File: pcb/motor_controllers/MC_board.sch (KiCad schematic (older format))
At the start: 22 parts, among them J1 Screw_Terminal_01x08, U1 Teensy3.2

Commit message: Added analog output RJ45 and audio amplifier symbol.
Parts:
- removed 5VGNDTEST1, 5VTEST1, 9VGNDTEST1, 9VTEST1: TestPoint, TestPoint:TestPoint_Plated_Hole_D5.0mm, symbol Connector:TestPoint
- removed C2, C3, C4: 100 uF, Capacitor_THT:C_Rect_L7.2mm_W7.2mm_P5.00mm_FKS2_FKP2_MKS2_MKP2, symbol Device:CP1
- added 12V1: 12V, Connector_BarrelJack:BarrelJack_Horizontal, symbol Connector:Barrel_Jack
- added J2: RJ45, symbol Connector:RJ45
- added U2: MAX98306, spatialsparrow:MAX98306, symbol spatialsparrow:MAX98306
- 5V1: value Barrel_Jack -> 5V
- 9V1: value Barrel_Jack -> 9V
- U1: footprint Teensey:Teensy30_31_32_LC -> lib:Teensy30_31_32_LC; symbol teensey:Teensy3.2 -> teensy:Teensy3.2
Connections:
- net labels added: +5V, +9V, GND
- wire segments 213 -> 146
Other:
- note added: "Power connectors\n"
- note added: "Stimuli - analog output connection"
- note added: "Teensy controller and stepper motor drivers"
- moved on the sheet: 5V1, 9V1, C1, FromTouch1, FromZeros1, J1, LeverL-ToMotor1, LeverR-ToMotor1, MC-LeverL1, MC-LeverR1, MC-SpoutL1, MC-SpoutR1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

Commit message: Added pinout text to kicad
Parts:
- renumbered LeverL-ToMotor1 to HandleL-ToMotor1, LeverR-ToMotor1 to HandleR-ToMotor1
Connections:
- net at MC-SpoutR1.3 (A2): now also MC-SpoutR1.4 (A1), SpoutR-ToMotor1.1 (Pin_1); no longer SpoutR-ToMotor1.2 (Pin_2)
- net at HandleR-ToMotor1.2 (Pin_2), MC-LeverR1.3 (A2): now also HandleR-ToMotor1.4 (Pin_4), MC-LeverR1.4 (A1), MC-LeverR1.6 (B2)
- net at HandleR-ToMotor1.1 (Pin_1): now also HandleR-ToMotor1.3 (Pin_3), MC-LeverR1.5 (B1); no longer MC-LeverR1.4 (A1)
- net at J1.7 (Pin_7), U1.27 (20_A6_CS_PWM): now also FromTouch1.1 (Pin_1), U1.30 (23_A9_Touch_PWM)
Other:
- note added: "INPUT PINS\n// Inputs for lick sensors\nLEVERSENSOR_L 15 // touch line for lever touch\nLEVERSENSOR_R 16 // touch line for lever touch\nSPOUTSENSOR_L 22 // touch line for left spout\nSPOUTSENSOR_R 23 // touch line for right spout\n// Pins for stepper - spouts\nPIN_SPOUTOUT_L 5\nPIN_SPOUTOUT_R 6\nPIN_SPOUTSTEP_L 13\nPIN_SPOUTDIR_L 14\nPIN_SPOUTSTEP_R 17\nPIN_SPOUTDIR_R 18\n// Pins for stepper - ha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"
- note added: "Stepper motor drivers\nHandles and Spout motors\n"
- note removed: "Teensy controller and stepper motor drivers"
- moved on the sheet: HandleL-ToMotor1, HandleR-ToMotor1, MC-LeverL1, MC-LeverR1, MC-SpoutL1, MC-SpoutR1, SpoutL-ToMotor1, SpoutR-ToMotor1, U1

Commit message: Pinout added and rj45
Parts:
- added J?: Screw_Terminal_01x02, symbol Connector:Screw_Terminal_01x02
- added SoundVision: Screw_Terminal_01x06, TerminalBlock_TE-Connectivity:TerminalBlock_TE_282825-4_1x06_P5.08mm_Horizontal, symbol Connector:Screw_Terminal_01x05
- FromTouch1, FromZeros1: symbol Connector:Screw_Terminal_01x04 -> Connector:Screw_Terminal_01x05
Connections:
- net at MC-SpoutL1.15 (STEP): no longer U1.20 (13_LED_SCK)
- net at MC-SpoutL1.16 (DIR): no longer U1.21 (14_A0_SCK)
- net at MC-SpoutL1.3 (A2): no longer SpoutL-ToMotor1.2 (Pin_2)
- net at MC-SpoutL1.4 (A1): no longer SpoutL-ToMotor1.1 (Pin_1)
- net at MC-SpoutL1.5 (B1): no longer SpoutL-ToMotor1.3 (Pin_3)
- net at MC-SpoutL1.6 (B2): no longer SpoutL-ToMotor1.4 (Pin_4)
- net at MC-SpoutR1.15 (STEP): no longer U1.24 (17_A3_SDA0_Touch)
- net at MC-SpoutR1.16 (DIR): no longer U1.25 (18_A4_SDA0_Touch)
- net at MC-SpoutR1.5 (B1): no longer SpoutR-ToMotor1.3 (Pin_3)
- net at MC-SpoutR1.6 (B2): no longer SpoutR-ToMotor1.4 (Pin_4)
- net at MC-LeverL1.15 (STEP): no longer U1.12 (10_TX2_CS_PWM)
- net at MC-LeverL1.3 (A2): no longer HandleL-ToMotor1.2 (Pin_2)
- net at MC-LeverL1.4 (A1): no longer HandleL-ToMotor1.1 (Pin_1)
- net at MC-LeverL1.5 (B1): no longer HandleL-ToMotor1.3 (Pin_3)
- net at MC-LeverL1.6 (B2): no longer HandleL-ToMotor1.4 (Pin_4)
- net at MC-LeverL1.9 (~EN): no longer U1.11 (9_RX2_CS_PWM)
- net at MC-LeverR1.15 (STEP): no longer U1.13 (11_DOUT)
- net at MC-LeverR1.16 (DIR): no longer U1.14 (12_DIN)
- net at U1.10 (8_TX3_DIN): no longer FromZeros1.1 (Pin_1)
- net at U1.2 (0_RX1_Touch): no longer J1.1 (Pin_1)
- net at U1.22 (15_A1_CS_Touch): no longer FromTouch1.4 (Pin_4)
- net at U1.23 (16_A2_SCL0_Touch): no longer FromTouch1.3 (Pin_3)
- net at U1.26 (19_A5_SCL0_Touch): no longer J1.6 (Pin_6)
- net at U1.28 (21_A7_RX1_CS_PWM): no longer J1.8 (Pin_8)
- net at U1.29 (22_A8_Touch_PWM): no longer FromTouch1.2 (Pin_2)
- net at U1.3 (1_TX1_Touch): no longer J1.2 (Pin_2)
- net at U1.4 (2): no longer J1.3 (Pin_3)
- net at U1.5 (3_TX_PWM): no longer J1.4 (Pin_4)
- net at U1.6 (4_RX_PWM): no longer J1.5 (Pin_5)
- net at U1.7 (5_TX1_PWM): no longer FromZeros1.4 (Pin_4)
- net at U1.8 (6_PWM): no longer FromZeros1.3 (Pin_3)
- net at U1.9 (7_RX3_DOUT): no longer FromZeros1.2 (Pin_2)
- now unconnected: FromTouch1.1 (Pin_1), HandleR-ToMotor1.1 (Pin_1), HandleR-ToMotor1.2 (Pin_2), HandleR-ToMotor1.3 (Pin_3), HandleR-ToMotor1.4 (Pin_4), J1.7 (Pin_7), MC-LeverR1.3 (A2), MC-LeverR1.4 (A1), MC-LeverR1.5 (B1), MC-LeverR1.6 (B2), MC-SpoutR1.3 (A2), MC-SpoutR1.4 (A1), SpoutR-ToMotor1.1 (Pin_1), U1.27 (20_A6_CS_PWM), U1.30 (23_A9_Touch_PWM)
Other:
- moved on the sheet: C1, HandleL-ToMotor1, HandleR-ToMotor1, MC-LeverL1, MC-LeverR1, MC-SpoutL1, MC-SpoutR1, SpoutL-ToMotor1, SpoutR-ToMotor1

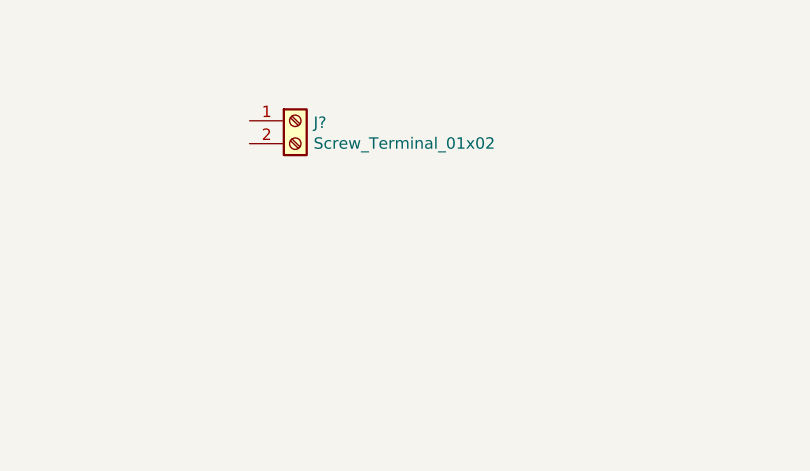
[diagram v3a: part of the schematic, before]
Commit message: text on screw terminal
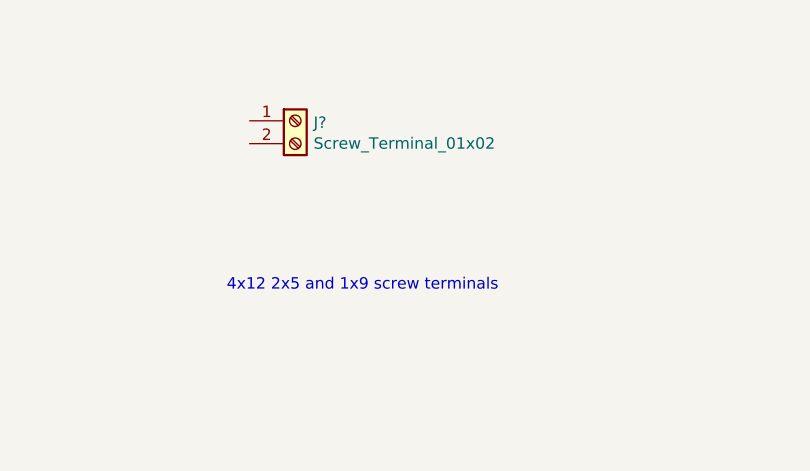
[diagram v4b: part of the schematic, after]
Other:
- note added: "4x12 2x5 and 1x9 screw terminals"
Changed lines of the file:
@@
 	1    0    0    -1
 $EndComp
+Text Notes 5000 13350 0    50   ~ 0
+4x12 2x5 and 1x9 screw terminals
 $EndSCHEMATC

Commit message: ran connections and did board layout
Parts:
- removed J1: Screw_Terminal_01x08, symbol Connector:Screw_Terminal_01x08
- added J12V1, J12V3, J12V4, J5V1, J5V2, J9V1: Screw_Terminal_01x02, teensey:TerminalBlock_TE_282825-2_1x02_P5.08mm_Horizontal, symbol Connector:Screw_Terminal_01x02
- added SoundVisionL1: Screw_Terminal_01x06, teensey:TerminalBlock_TE_282825-6_1x06_P5.08mm_Horizontal, symbol Connector:Screw_Terminal_01x06
- added sync_trigger_out1: Screw_Terminal_01x05, teensey:TerminalBlock_TE_282825-5_1x05_P5.08mm_Horizontal, symbol Connector:Screw_Terminal_01x05
- HandleL-ToMotor1, HandleR-ToMotor1, SpoutL-ToMotor1, SpoutR-ToMotor1: footprint TerminalBlock_TE-Connectivity:TerminalBlock_TE_282825-4_1x04_P5.08mm_Horizontal -> teensey:TerminalBlock_TE_282825-4_1x04_P5.08mm_Horizontal
- J12V2: renamed from J?; footprint (none) -> teensey:TerminalBlock_TE_282825-2_1x02_P5.08mm_Horizontal
- J2: footprint (none) -> teensey:RJ45_sparkfun
- SoundVisionR1: renamed from SoundVision; footprint TerminalBlock_TE-Connectivity:TerminalBlock_TE_282825-4_1x06_P5.08mm_Horizontal -> teensey:TerminalBlock_TE_282825-6_1x06_P5.08mm_Horizontal; symbol Connector:Screw_Terminal_01x05 -> Connector:Screw_Terminal_01x06
- ToHandleL1: renamed from FromZeros1; value Screw_Terminal_01x04 -> Screw_Terminal_01x05; footprint TerminalBlock_TE-Connectivity:TerminalBlock_TE_282825-4_1x04_P5.08mm_Horizontal -> teensey:TerminalBlock_TE_282825-5_1x05_P5.08mm_Horizontal
- ToHandleR1: renamed from FromTouch1; value Screw_Terminal_01x04 -> Screw_Terminal_01x05; footprint TerminalBlock_TE-Connectivity:TerminalBlock_TE_282825-4_1x04_P5.08mm_Horizontal -> teensey:TerminalBlock_TE_282825-5_1x05_P5.08mm_Horizontal
- U1: symbol teensy:Teensy3.2 -> MC_board-rescue:Teensy3.2-teensy
- U2: symbol spatialsparrow:MAX98306 -> MC_board-rescue:MAX98306-spatialsparrow
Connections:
- net +5V: now also 5V1.1, J5V1.1 (Pin_1), J5V2.1 (Pin_1); no longer U2.1 (VDD)
- net +9V: now also J9V1.1 (Pin_1)
- net GND: now also 12V1.1, 5V1.2, J12V2.2 (Pin_2), SoundVisionR1.5 (Pin_5), ToHandleL1.3 (Pin_3), ToHandleL1.5 (Pin_5), ToHandleR1.3 (Pin_3), ToHandleR1.5 (Pin_5), J12V1.2 (Pin_2), J12V3.2 (Pin_2), J12V4.2 (Pin_2), J5V1.2 (Pin_2), J5V2.2 (Pin_2), J9V1.2 (Pin_2), SoundVisionL1.5 (Pin_5)
- net at MC-SpoutL1.15 (STEP): now also U1.20 (13_LED_SCK)
- net at MC-SpoutL1.16 (DIR): now also U1.21 (14_A0_SCK)
- net at MC-SpoutL1.3 (A2): now also SpoutL-ToMotor1.2 (Pin_2)
- net at MC-SpoutL1.4 (A1): now also SpoutL-ToMotor1.1 (Pin_1)
- net at MC-SpoutL1.5 (B1): now also SpoutL-ToMotor1.3 (Pin_3)
- net at MC-SpoutL1.6 (B2): now also SpoutL-ToMotor1.4 (Pin_4)
- net at MC-SpoutR1.15 (STEP): now also U1.24 (17_A3_SDA0_Touch)
- net at MC-SpoutR1.16 (DIR): now also U1.25 (18_A4_SDA0_Touch)
- net at MC-SpoutR1.3 (A2): now also SpoutR-ToMotor1.2 (Pin_2)
- net at MC-SpoutR1.4 (A1): now also SpoutR-ToMotor1.1 (Pin_1)
- net at MC-SpoutR1.5 (B1): now also SpoutR-ToMotor1.3 (Pin_3)
- net at MC-SpoutR1.6 (B2): now also SpoutR-ToMotor1.4 (Pin_4)
- net at MC-LeverL1.15 (STEP): now also U1.11 (9_RX2_CS_PWM)
- net at MC-LeverL1.16 (DIR): now also U1.12 (10_TX2_CS_PWM)
- net at MC-LeverL1.3 (A2): now also HandleL-ToMotor1.2 (Pin_2)
- net at MC-LeverL1.4 (A1): now also HandleL-ToMotor1.1 (Pin_1)
- net at MC-LeverL1.5 (B1): now also HandleL-ToMotor1.3 (Pin_3)
- net at MC-LeverL1.6 (B2): now also HandleL-ToMotor1.4 (Pin_4)
- net at MC-LeverR1.15 (STEP): now also U1.13 (11_DOUT)
- net at MC-LeverR1.16 (DIR): now also U1.14 (12_DIN)
- net at MC-LeverR1.3 (A2): now also HandleR-ToMotor1.2 (Pin_2)
- net at MC-LeverR1.4 (A1): now also HandleR-ToMotor1.1 (Pin_1)
- net at MC-LeverR1.5 (B1): now also HandleR-ToMotor1.3 (Pin_3)
- net at MC-LeverR1.6 (B2): now also HandleR-ToMotor1.4 (Pin_4)
- net at U1.10 (8_TX3_DIN): now also ToHandleR1.4 (Pin_4)
- net at U1.22 (15_A1_CS_Touch): now also ToHandleL1.1 (Pin_1)
- net at U1.23 (16_A2_SCL0_Touch): now also ToHandleR1.1 (Pin_1)
- net at U1.26 (19_A5_SCL0_Touch): now also sync_trigger_out1.1 (Pin_1)
- net at U1.27 (20_A6_CS_PWM): now also sync_trigger_out1.2 (Pin_2)
- net at U1.28 (21_A7_RX1_CS_PWM): now also sync_trigger_out1.3 (Pin_3)
- net at U1.29 (22_A8_Touch_PWM): now also SoundVisionL1.1 (Pin_1)
- net at U1.30 (23_A9_Touch_PWM): now also SoundVisionR1.1 (Pin_1)
- net at U1.5 (3_TX_PWM): now also sync_trigger_out1.5 (Pin_5)
- net at U1.6 (4_RX_PWM): now also sync_trigger_out1.4 (Pin_4)
- net at U1.7 (5_TX1_PWM): now also SoundVisionL1.4 (Pin_4)
- net at U1.8 (6_PWM): now also SoundVisionR1.4 (Pin_4)
- net at U1.9 (7_RX3_DOUT): now also ToHandleL1.4 (Pin_4)
- net at ToHandleL1.2 (Pin_2): now also J2.7
- net at ToHandleR1.2 (Pin_2): now also J2.8
- net at SoundVisionR1.2 (Pin_2): now also U2.12 (R+)
- net at SoundVisionR1.3 (Pin_3): now also U2.13 (ROUT-)
- net +12V: now reaches J12V2.1 (Pin_1)
- net +12V: now also 12V1.2, J12V1.1 (Pin_1), J12V3.1 (Pin_1), J12V4.1 (Pin_1)
- net at U2.10 (LOUT-): now also SoundVisionL1.3 (Pin_3)
- net at U2.11 (LOUT+): now also SoundVisionL1.2 (Pin_2)
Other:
- note added: "1- Handle Touch\n2- Actuator +\n3- Actuator - (GND)\n4- Handle Out\n5- Handle Zero (GND)"
- note added: "1- Spout Touch\n2- Audio +\n3- Audio - \n4- Spout Out\n5- Spout Zero (GND)\n6- Visual trigger"
- note added: "2- left audio\n3- right audio\n4-\n5- \n6- \n7- left actuator+\n8- right actuator+"
- moved on the sheet: 12V1, 5V1, 9V1

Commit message: Filled areas on pcb for controller.
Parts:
- added C2, C3, C4: 100 uF, Capacitor_THT:C_Rect_L7.2mm_W7.2mm_P5.00mm_FKS2_FKP2_MKS2_MKP2, symbol Device:CP1
- added distractor1: Screw_Terminal_01x02, teensey:TerminalBlock_TE_282825-2_1x02_P5.08mm_Horizontal, symbol Connector:Screw_Terminal_01x02
- U1: footprint lib:Teensy30_31_32_LC -> teensey:Teensy30_31_32_LC
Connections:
- net +5V: now also U2.1 (VDD)
- net +9V: now also C2.1, C3.1, C4.1
- net GND: now also U1.17 (GND), distractor1.1 (Pin_1); no longer 9V1.2, C1.2, J9V1.2 (Pin_2), MC-LeverL1.7 (GND), MC-LeverR1.7 (GND), MC-SpoutL1.7 (GND), MC-SpoutR1.7 (GND)
- net at ToHandleL1.2 (Pin_2): now also J2.6; no longer J2.7
- net at ToHandleR1.2 (Pin_2): now also J2.7; no longer J2.8
- net at SoundVisionR1.6 (Pin_6): now also J2.5
- net at SoundVisionL1.6 (Pin_6): now also J2.4
- new net: J2.8, distractor1.2 (Pin_2)
- new net GND1: 9V1.2, C1.2, C2.2, C3.2, C4.2, J9V1.2 (Pin_2), MC-LeverL1.7 (GND), MC-LeverR1.7 (GND), MC-SpoutL1.7 (GND), MC-SpoutR1.7 (GND)
- no-connect marks 0 -> 55
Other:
- note added: "2- left audio\n3- right audio\n4- left vision\n5- right vision\n6- left handle actuator\n7- right handle actuator\n8- distractor"
- note removed: "2- left audio\n3- right audio\n4-\n5- \n6- \n7- left actuator+\n8- right actuator+"
- moved on the sheet: HandleL-ToMotor1, HandleR-ToMotor1, SpoutL-ToMotor1, SpoutR-ToMotor1
